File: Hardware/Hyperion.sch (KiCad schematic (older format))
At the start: 0 parts

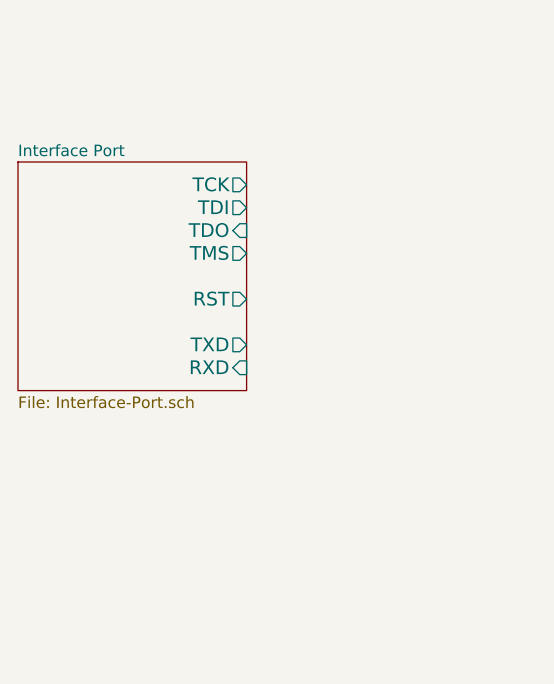
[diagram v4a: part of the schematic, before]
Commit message: Add RBF switch prototype
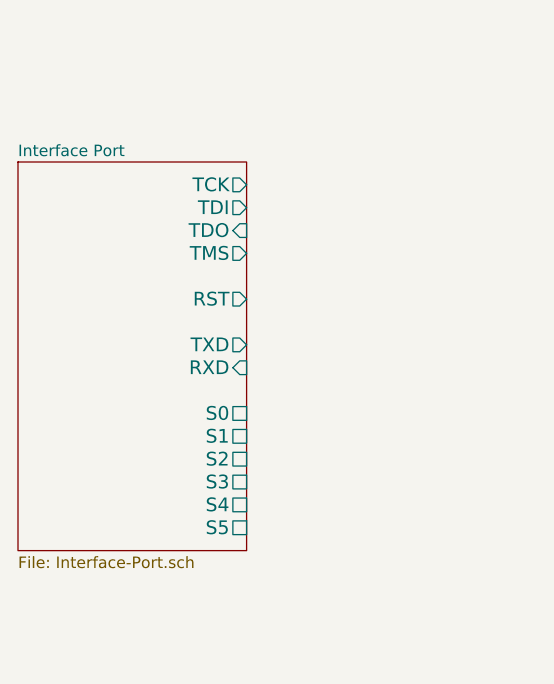
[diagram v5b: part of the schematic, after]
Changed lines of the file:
@@
 Sheet 1 4
 Title "Hyperion"
-Date "2 may 2014"
+Date "4 may 2014"
 Rev "0.2"
 Comp "Aerodyne Labs"
@@
 $EndSheet
 $Sheet
-S 1800 3200 1000 1000
+S 1800 3200 1000 1700
 U 530DB905
 F0 "Interface Port" 50
@@
 F7 "RXD" I R 2800 4100 60
 F8 "RST" O R 2800 3800 60
+F9 "S2" U R 2800 4500 60
+F10 "S3" U R 2800 4600 60
+F11 "S4" U R 2800 4700 60
+F12 "S5" U R 2800 4800 60
+F13 "S1" U R 2800 4400 60
+F14 "S0" U R 2800 4300 60
 $EndSheet
 $Sheet
